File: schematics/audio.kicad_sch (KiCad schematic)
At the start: 8 parts, among them J5 Left Audio, J6 Right Audio, U12 EN5503DOC, U17 41464, U18 41464, U19 41464, U20 41464

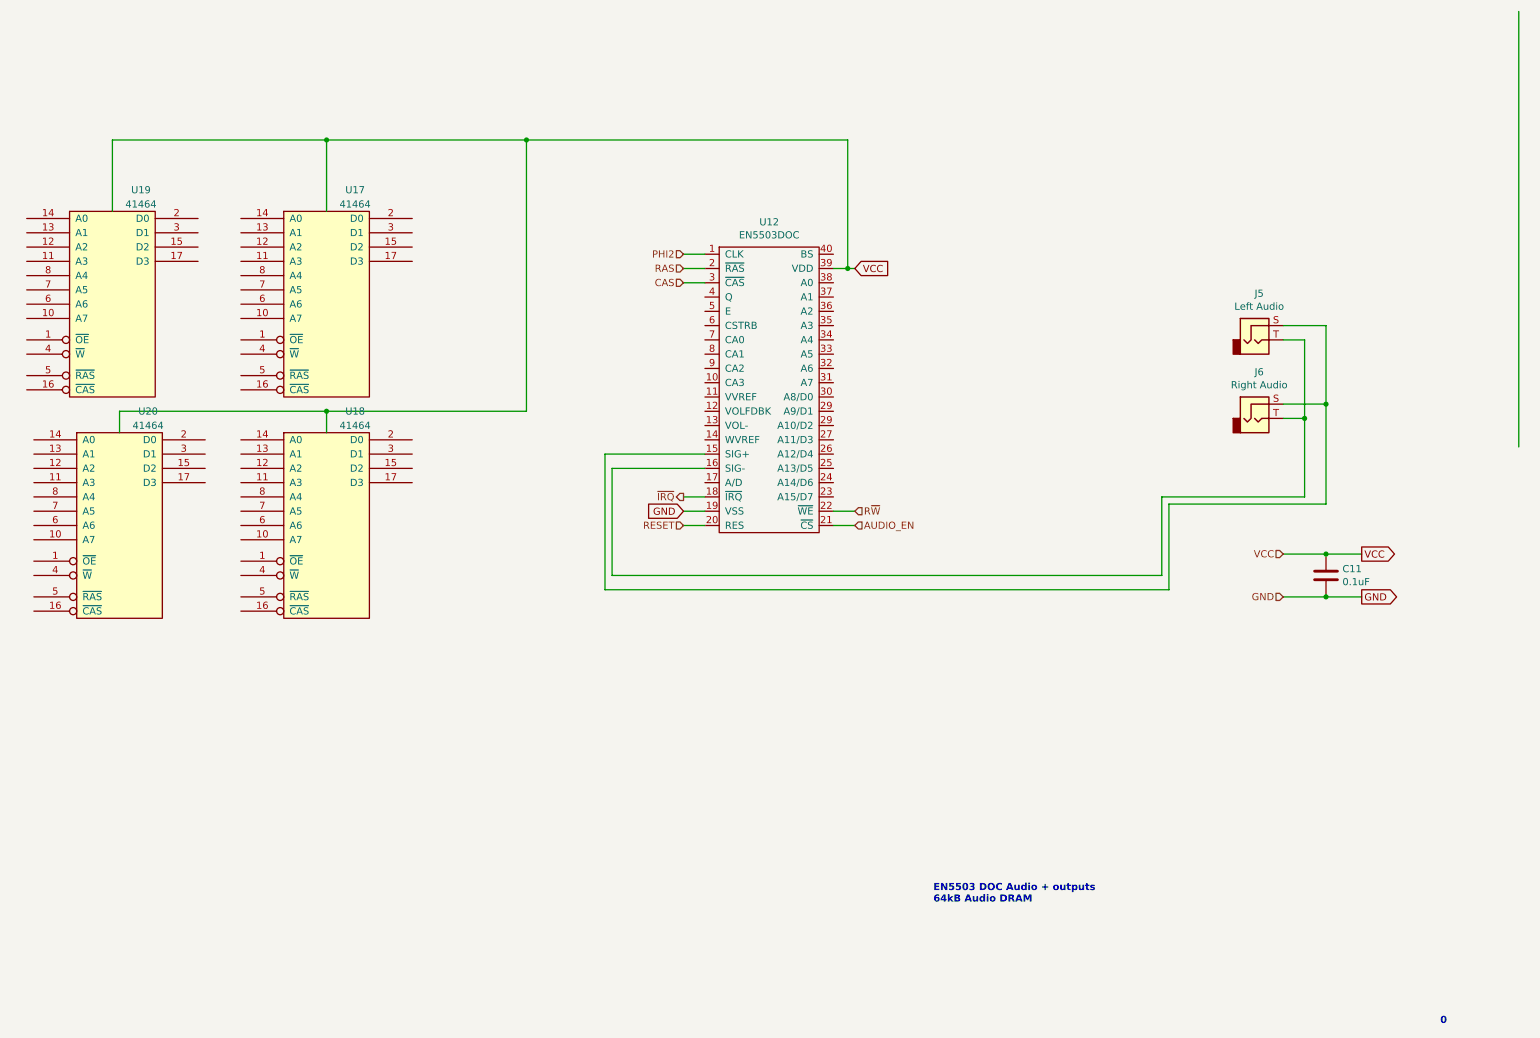
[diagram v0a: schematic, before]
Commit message: Small tweaks here and there. Added a lot of missing footprint definitions.
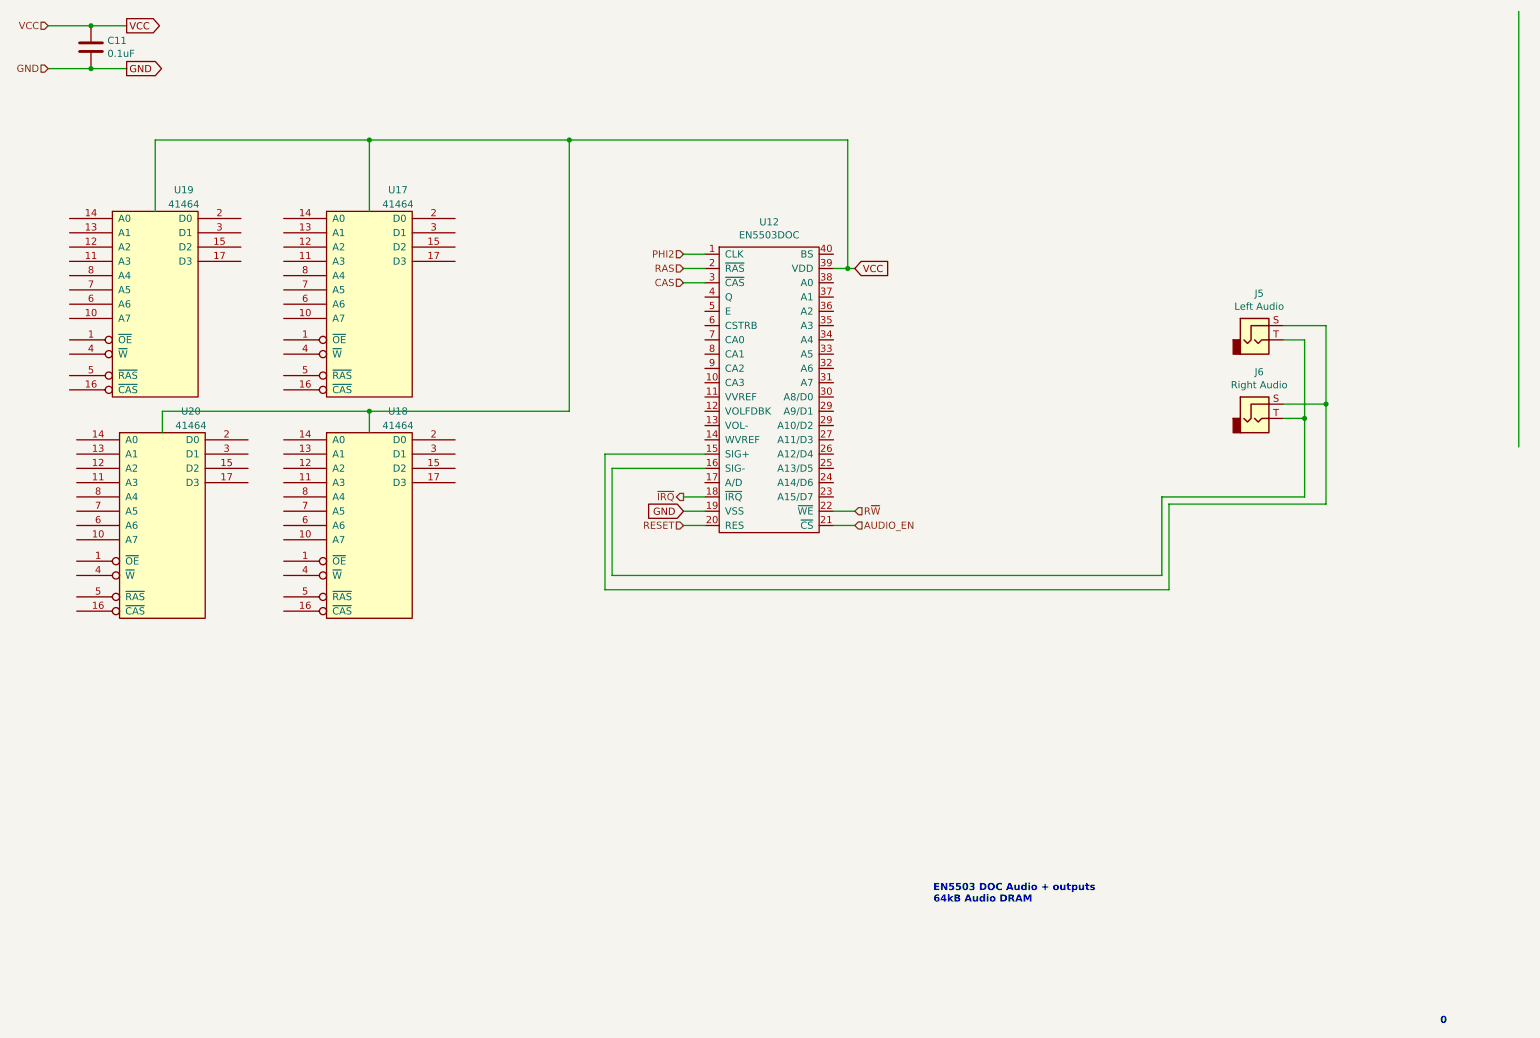
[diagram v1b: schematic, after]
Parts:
- C11: footprint (none) -> Capacitor_THT:CP_Radial_D4.0mm_P1.50mm
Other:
- moved on the sheet: C11, U17, U18, U19, U20

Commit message: Added analog audio section. Followed Apple IIGS schematics for this one as it uses the same EN5503DOC audio chip. Still a bit unclear how to connect the RCA jacks instead of the phonejack and analog ground is not connected.
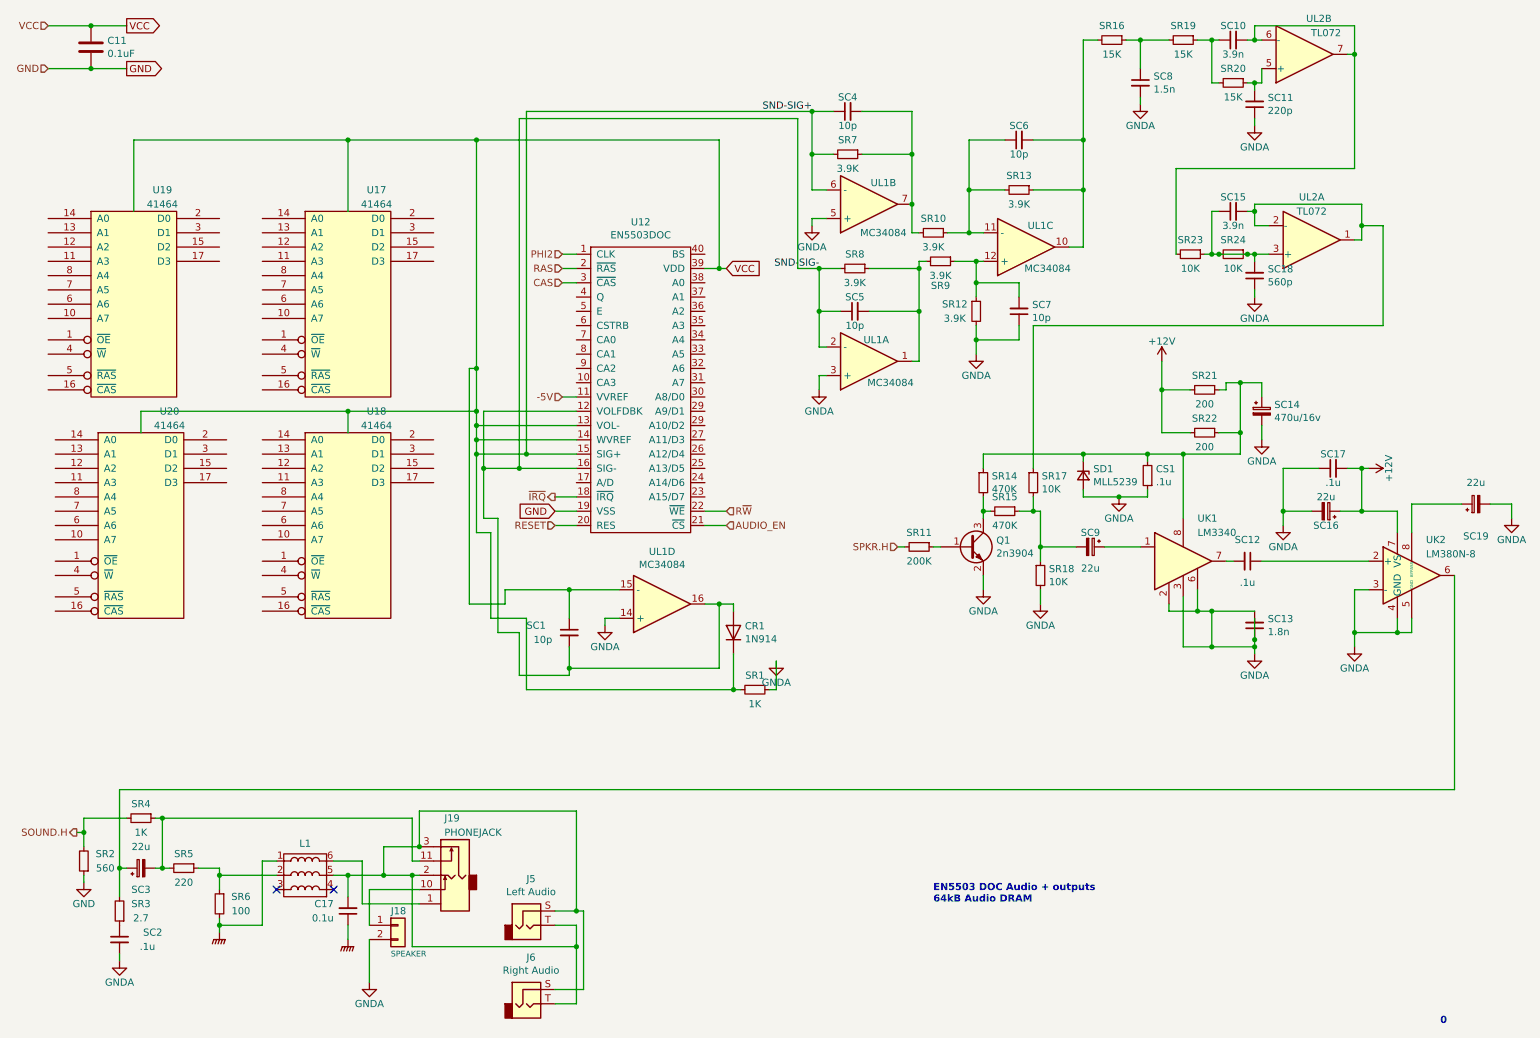
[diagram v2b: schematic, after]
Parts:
- added C17: 0.1u, symbol Device:C_Small
- added CR1: 1N914, Diode_THT:D_DO-35_SOD27_P7.62mm_Horizontal, symbol Diode:1N914
- added CS1: .1u, symbol Device:R_Small
- added J18: SPEAKER, Connector_PinHeader_2.54mm:PinHeader_1x02_P2.54mm_Vertical, symbol Connector_Generic:Conn_01x02
- added J19: PHONEJACK, symbol IIgs-Schematic:Audio_Phone_Jack-IIgs
- added L1: L-Pack3, symbol IIgs-Schematic:L-Pack3
- added Q1: 2n3904, symbol Device:Q_NPN_BEC
- added SC1, SC4, SC5, SC6, SC7: 10p, symbol Device:C_Small
- added SC10, SC15: 3.9n, symbol Device:C_Small
- added SC11: 220p, symbol Device:C_Small
- added SC12, SC17, SC2: .1u, symbol Device:C_Small
- added SC13: 1.8n, symbol Device:C_Small
- added SC14: 470u/16v, symbol Device:C_Polarized_Small
- added SC16, SC19, SC3, SC9: 22u, symbol Device:C_Polarized_Small
- added SC18: 560p, symbol Device:C_Small
- added SC8: 1.5n, symbol Device:C_Small
- added SD1: MLL5239, symbol Device:D_Zener_Small
- added SR1, SR4: 1K, symbol Device:R_Small
- added SR10, SR12, SR13, SR7, SR8, SR9: 3.9K, symbol Device:R_Small
- added SR11: 200K, symbol Device:R_Small
- added SR14, SR15: 470K, symbol Device:R_Small
- added SR16, SR19, SR20: 15K, symbol Device:R_Small
- added SR17, SR18, SR23, SR24: 10K, symbol Device:R_Small
- added SR2: 560, symbol Device:R_Small
- added SR21, SR22: 200, symbol Device:R_Small
- added SR3: 2.7, symbol Device:R_Small
- added SR5: 220, symbol Device:R_Small
- added SR6: 100, symbol Device:R_Small
- added UK1: LM3340, symbol IIgs-Schematic:LM3340
- added UK2: LM380N-8, Package_DIP:DIP-8_W7.62mm, symbol Amplifier_Audio:LM380N-8
- added UL1: MC34084, symbol IIgs-Schematic:MC34084
- added UL2: TL072, symbol Amplifier_Operational:TL072
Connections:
- net GND: now also SR2.1
- net VCC: now also U12.13 (VOL-), U12.14 (WVREF), U12.15 (SIG+), CR1.1 (K), SC1.1, SC4.1, SR1.2, SR7.2, UL1.15 (-), UL1.6 (-)
- net -5V: now reaches U12.11 (VVREF)
- net SND-SIG-: now reaches U12.12 (VOLFDBK)
- net SND-SIG-: now also U12.16 (SIG-), CR1.2 (A), SC1.2, SC5.1, SR8.2, UL1.16, UL1.2 (-)
- net at J5.S, J6.S: now also J5.T, J6.T, C17.2, J19.2, J19.3, L1.5; no longer U12.15 (SIG+)
- new net: L1.2, SR5.1, SR6.1
- new net: SC6.2, SR13.1, SR16.2, UL1.10
- new net: SC6.1, SR10.1, SR13.2, UL1.11 (-)
- new net: SC7.2, SR12.1, SR9.1, UL1.12 (+)
- new net: SC10.1, SR19.1, SR20.2
- new net: SC10.2, SR23.2, UL2.6 (-), UL2.7
- new net: SC5.2, SR8.1, SR9.2, UL1.1
- new net: CS1.2, SC14.1, SD1.1 (K), SR14.1, SR21.1, SR22.1, UK1.8
- new net: SC3.1, SR3.2, UK2.6
- new net: J19.11, SC3.2, SR4.1, SR5.2
- new net: SC15.1, SC18.2, SR23.1, SR24.1, SR24.2, UL2.3 (+)
- new net: SC4.2, SR10.2, SR7.1, UL1.7
- new net: SC2.1, SR3.1
- new net: SC19.1, UK2.8 (BYPASS)
- new net: SC9.1, UK1.1
- new net: SC12.2, UK1.7
- new net: SC11.2, SR20.1, UL2.5 (+)
- new net: Q1.1 (B), SR11.1
- new net: SC15.2, SR17.1, UL2.1, UL2.2 (-)
- new net: SC9.2, SR15.1, SR17.2, SR18.1
- new net: SC8.1, SR16.1, SR19.2
- new net: J19.1, L1.6
- new net: J18.1 (Pin_1), J19.10
- new net: Q1.3 (C), SR14.2, SR15.2
- new net: SC12.1, UK2.2 (+)
- new net +12V: SC16.1, SC17.2, SR21.2, SR22.2, UK2.7 (VS)
- new net GNDA: CS1.1, J18.2 (Pin_2), Q1.2 (E), SC11.1, SC13.1, SC13.2, SC14.2, SC16.2, SC17.1, SC18.1, SC19.2, SC2.2, SC7.1, SC8.2, SD1.2 (A), SR1.1, SR12.2, SR18.2, UK1.2, UK1.3, UK1.6, UK2.3 (-), UK2.4 (GND), UK2.5 (GND), UL1.14 (+), UL1.3 (+), UL1.5 (+)
- new net GNDPWR: C17.1, L1.1, SR6.2
- new net SOUND.H: SR2.2, SR4.2
- new net SPKR.H: SR11.2
- no-connect marks 0 -> 2
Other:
- moved on the sheet: J5, J6, U12, U17, U18, U19, U20
